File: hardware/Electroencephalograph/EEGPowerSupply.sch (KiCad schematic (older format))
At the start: 25 parts, among them U6 TPS60403, U7 LP5912-1.8DRVT, U8 LP5912-1.8DRVT, U9 LP5912-1.8DRVT

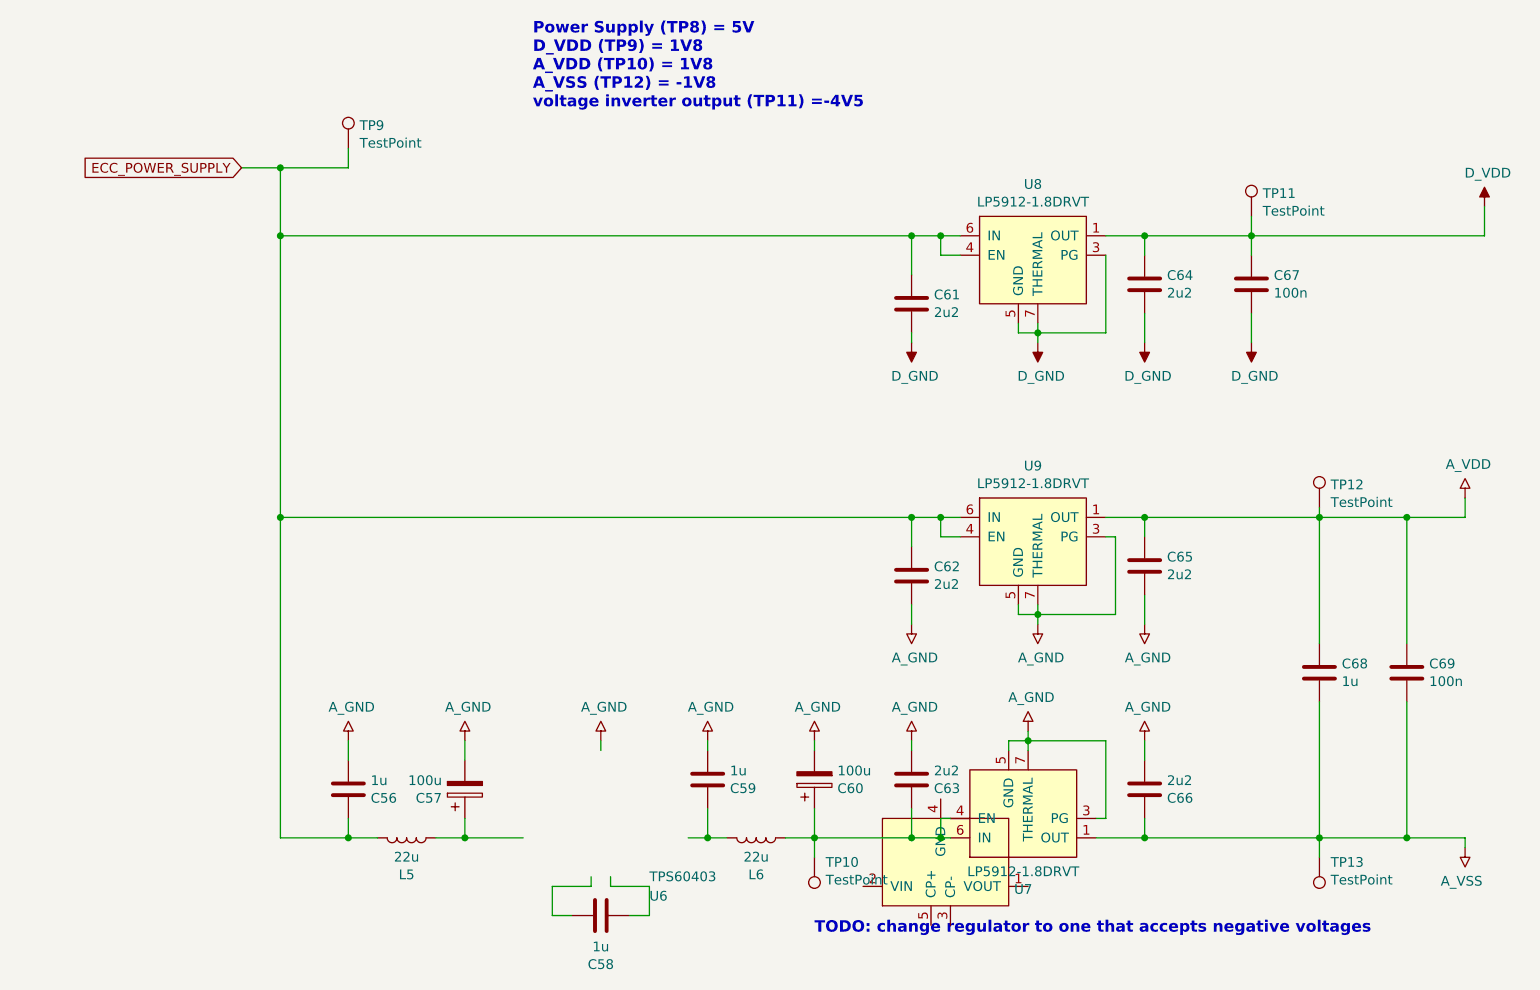
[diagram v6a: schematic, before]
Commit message: placing components groups
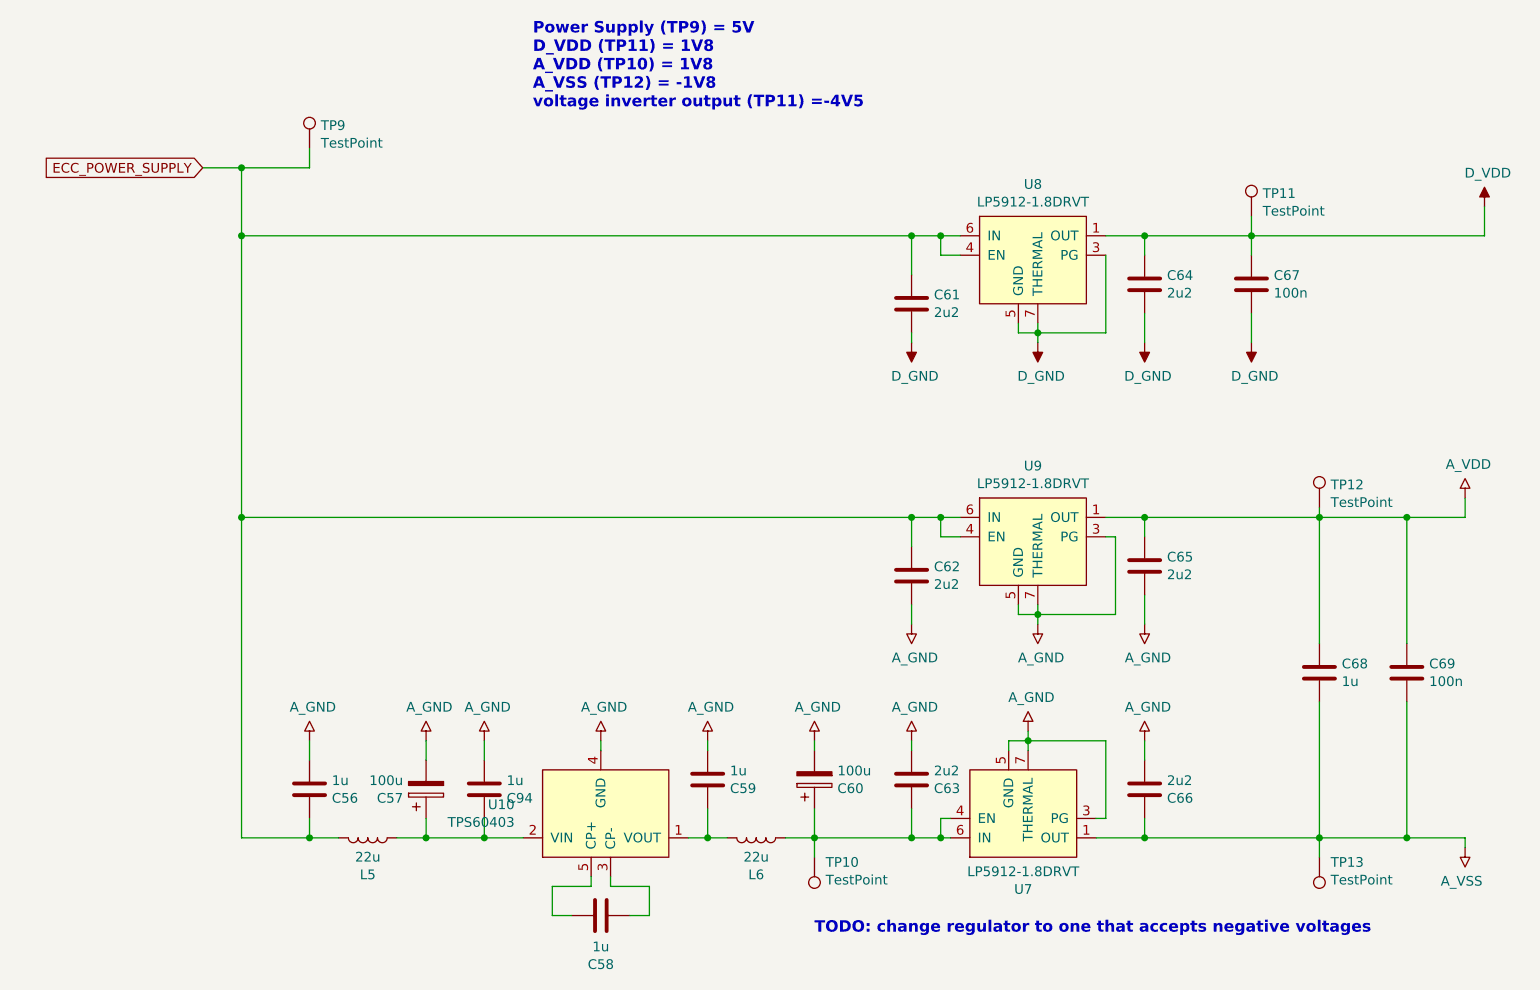
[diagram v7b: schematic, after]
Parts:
- removed U6: TPS60403, Package_SO:SOP-8_3.76x4.96mm_P1.27mm, symbol Electroencephalograph:TPS60403
- added C94: 1u, Capacitor_SMD:C_0402_1005Metric, symbol Device:C
- added U10: TPS60403, Package_TO_SOT_SMD:SOT-23-5, symbol Electroencephalograph:TPS60403
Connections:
- wire segments 101 -> 104
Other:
- note added: "Power Supply (TP9) = 5V\nD_VDD (TP11) = 1V8\nA_VDD (TP10) = 1V8\nA_VSS (TP12) = -1V8\nvoltage inverter output (TP11) =-4V5"
- note removed: "Power Supply (TP8) = 5V\nD_VDD (TP9) = 1V8\nA_VDD (TP10) = 1V8\nA_VSS (TP12) = -1V8\nvoltage inverter output (TP11) =-4V5"
- moved on the sheet: C56, C57, L5, TP9
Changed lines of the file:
@@
 $EndDescr
-$Comp
-L Electroencephalograph:TPS60403 U?
-U 1 1 5E0A0C58
-P 5450 5650
-AR Path="/5DFE0AD6/5E0A0C58" Ref="U?"  Part="1"
-AR Path="/5E0992D6/5E0A0C58" Ref="U6"  Part="1"
-F 0 "U6" H 3950 5800 50  0000 L CNN
-F 1 "TPS60403" H 3950 5700 50  0000 L CNN
-F 2 "Package_SO:SOP-8_3.76x4.96mm_P1.27mm" H 5450 5650 50  0001 C CNN
-F 3 "" H 5450 5650 50  0001 C CNN
-	1    5450 5650
-	1    0    0    1
-$EndComp
 $Comp
 L Device:C C?
@@
 	3750 5750 3750 5700
 Wire Wire Line
-	3300 5500 3000 5500
+	3300 5500 3100 5500
 Wire Wire Line
 	4150 5500 4250 5500
@@
 	4250 5000 4250 5050
 Wire Wire Line
-	3000 5500 3000 5400
-Wire Wire Line
-	3000 5000 3000 5100
+	2800 5500 2800 5400
+Wire Wire Line
+	2800 5000 2800 5100
 $Comp
 L Electroencephalograph:A_GND #PWR?
 U 1 1 5E0A0C8E
-P 3000 5000
+P 2800 5000
 AR Path="/5DFE0AD6/5E0A0C8E" Ref="#PWR?"  Part="1"
 AR Path="/5E0992D6/5E0A0C8E" Ref="#PWR111"  Part="1"
-F 0 "#PWR111" H 3000 5025 50  0001 C CNN
-F 1 "A_GND" H 3017 4827 50  0000 C CNN
-F 2 "" H 3000 5025 50  0001 C CNN
-F 3 "" H 3000 5025 50  0001 C CNN
-	1    3000 5000
+F 0 "#PWR111" H 2800 5025 50  0001 C CNN
+F 1 "A_GND" H 2817 4827 50  0000 C CNN
+F 2 "" H 2800 5025 50  0001 C CNN
+F 3 "" H 2800 5025 50  0001 C CNN
+	1    2800 5000
 	1    0    0    1
 $EndComp
@@
 L Device:C C?
 U 1 1 5E0A0C94
-P 2400 5250
+P 2200 5250
 AR Path="/5DF4CFF8/5E0A0C94" Ref="C?"  Part="1"
 AR Path="/5DF61103/5E0A0C94" Ref="C?"  Part="1"
 AR Path="/5DFE0AD6/5E0A0C94" Ref="C?"  Part="1"
 AR Path="/5E0992D6/5E0A0C94" Ref="C56"  Part="1"
-F 0 "C56" H 2515 5296 50  0000 L CNN
-F 1 "1u" H 2515 5205 50  0000 L CNN
-F 2 "Capacitor_SMD:C_0402_1005Metric" H 2438 5100 50  0001 C CNN
-F 3 "~" H 2400 5250 50  0001 C CNN
-	1    2400 5250
+F 0 "C56" H 2315 5296 50  0000 L CNN
+F 1 "1u" H 2315 5205 50  0000 L CNN
+F 2 "Capacitor_SMD:C_0402_1005Metric" H 2238 5100 50  0001 C CNN
+F 3 "~" H 2200 5250 50  0001 C CNN
+	1    2200 5250
 	1    0    0    1
 $EndComp
@@
 L Device:CP C?
 U 1 1 5E0A0C9A
-P 3000 5250
+P 2800 5250
 AR Path="/5DF4CFF8/5E0A0C9A" Ref="C?"  Part="1"
 AR Path="/5DF61103/5E0A0C9A" Ref="C?"  Part="1"
 AR Path="/5DFE0AD6/5E0A0C9A" Ref="C?"  Part="1"
 AR Path="/5E0992D6/5E0A0C9A" Ref="C57"  Part="1"
-F 0 "C57" H 2882 5296 50  0000 R CNN
-F 1 "100u" H 2882 5205 50  0000 R CNN
-F 2 "Capacitor_SMD:CP_Elec_6.3x5.8" H 3038 5100 50  0001 C CNN
-F 3 "~" H 3000 5250 50  0001 C CNN
-	1    3000 5250
+F 0 "C57" H 2682 5296 50  0000 R CNN
+F 1 "100u" H 2682 5205 50  0000 R CNN
+F 2 "Capacitor_SMD:CP_Elec_6.3x5.8" H 2838 5100 50  0001 C CNN
+F 3 "~" H 2800 5250 50  0001 C CNN
+	1    2800 5250
 	1    0    0    1
 $EndComp
@@
 L Electroencephalograph:A_GND #PWR?
 U 1 1 5E0A0CA6
-P 2400 5000
+P 2200 5000
 AR Path="/5DFE0AD6/5E0A0CA6" Ref="#PWR?"  Part="1"
 AR Path="/5E0992D6/5E0A0CA6" Ref="#PWR110"  Part="1"
-F 0 "#PWR110" H 2400 5025 50  0001 C CNN
-F 1 "A_GND" H 2417 4827 50  0000 C CNN
-F 2 "" H 2400 5025 50  0001 C CNN
-F 3 "" H 2400 5025 50  0001 C CNN
-	1    2400 5000
-	1    0    0    1
-$EndComp
-Wire Wire Line
-	2400 5000 2400 5100
-Wire Wire Line
-	2400 5400 2400 5500
+F 0 "#PWR110" H 2200 5025 50  0001 C CNN
+F 1 "A_GND" H 2217 4827 50  0000 C CNN
+F 2 "" H 2200 5025 50  0001 C CNN
+F 3 "" H 2200 5025 50  0001 C CNN
+	1    2200 5000
+	1    0    0    1
+$EndComp
+Wire Wire Line
+	2200 5000 2200 5100
+Wire Wire Line
+	2200 5400 2200 5500
 Wire Wire Line
 	4800 5500 4800 5350
@@
 Wire Wire Line
 	5300 5350 5300 5500
-Text GLabel 1850 2050 0    50   Input ~ 0
+Text GLabel 1650 2050 0    50   Input ~ 0
 ECC_POWER_SUPPLY
 $Comp
@@
 	5300 4000 5300 3850
 Wire Wire Line
-	1850 2050 2050 2050
-Wire Wire Line
-	2050 5500 2400 5500
-Wire Wire Line
-	2050 3850 5300 3850
-Connection ~ 2050 3850
-Wire Wire Line
-	2050 3850 2050 5500
+	1650 2050 1850 2050
+Wire Wire Line
+	1850 5500 2200 5500
+Wire Wire Line
+	1850 3850 5300 3850
+Connection ~ 1850 3850
+Wire Wire Line
+	1850 3850 1850 5500
 $Comp
 L Device:C C?
@@
 	8250 2400 8250 2250
 Wire Wire Line
-	5300 2400 2050 2400
-Wire Wire Line
-	2050 2050 2050 2400
+	5300 2400 1850 2400
+Wire Wire Line
+	1850 2050 1850 2400
 Connection ~ 5300 2400
-Connection ~ 2050 2400
-Wire Wire Line
-	2050 2400 2050 3850
+Connection ~ 1850 2400
+Wire Wire Line
+	1850 2400 1850 3850
 Connection ~ 5300 5500
 Wire Wire Line
@@
 L Device:L L?
 U 1 1 5E0C44DF
-P 2700 5500
+P 2500 5500
 AR Path="/5DFE0AD6/5E0C44DF" Ref="L?"  Part="1"
 AR Path="/5E0992D6/5E0C44DF" Ref="L5"  Part="1"
-F 0 "L5" V 2890 5500 50  0000 C CNN
-F 1 "22u" V 2799 5500 50  0000 C CNN
-F 2 "Electroencephalograph:L_7.3x7.3_H3.5" H 2700 5500 50  0001 C CNN
-F 3 "~" H 2700 5500 50  0001 C CNN
-	1    2700 5500
+F 0 "L5" V 2690 5500 50  0000 C CNN
+F 1 "22u" V 2599 5500 50  0000 C CNN
+F 2 "Electroencephalograph:L_7.3x7.3_H3.5" H 2500 5500 50  0001 C CNN
+F 3 "~" H 2500 5500 50  0001 C CNN
+	1    2500 5500
 	0    1    1    0
 $EndComp
 Wire Wire Line
-	2400 5500 2550 5500
-Connection ~ 2400 5500
-Wire Wire Line
-	2850 5500 3000 5500
-Connection ~ 3000 5500
+	2200 5500 2350 5500
+Connection ~ 2200 5500
+Wire Wire Line
+	2650 5500 2800 5500
+Connection ~ 2800 5500
 Wire Wire Line
 	6500 2400 7050 2400
@@
 Wire Wire Line
 	5950 4350 5950 4400
-Text Notes 3350 1750 0    59   ~ 12
-Power Supply (TP8) = 5V\nD_VDD (TP9) = 1V8\nA_VDD (TP10) = 1V8\nA_VSS (TP12) = -1V8\nvoltage inverter output (TP11) =-4V5
 $Comp
 L Electroencephalograph:A_GND #PWR?
@@
 	6250 5500 6500 5500
 Connection ~ 6500 5500
-$Comp
-L Connector:TestPoint TP?
-U 1 1 5E14A4FF
-P 2400 1950
-AR Path="/5DF61103/5E14A4FF" Ref="TP?"  Part="1"
-AR Path="/5E0992D6/5E14A4FF" Ref="TP9"  Part="1"
-F 0 "TP9" H 2458 2068 50  0000 L CNN
-F 1 "TestPoint" H 2458 1977 50  0000 L CNN
-F 2 "TestPoint:TestPoint_Pad_1.5x1.5mm" H 2600 1950 50  0001 C CNN
-F 3 "~" H 2600 1950 50  0001 C CNN
-	1    2400 1950
-	1    0    0    -1
-$EndComp
-Wire Wire Line
-	2050 2050 2400 2050
-Wire Wire Line
-	2400 2050 2400 1950
-Connection ~ 2050 2050
 Wire Wire Line
 	6500 5500 7400 5500
@@
 Text Notes 4800 6000 0    59   ~ 12
 TODO: change regulator to one that accepts negative voltages
+Wire Wire Line
+	2200 2050 2200 1950
+Connection ~ 1850 2050
+Wire Wire Line
+	1850 2050 2200 2050
+$Comp
+L Connector:TestPoint TP?
+U 1 1 5E14A4FF
+P 2200 1950
+AR Path="/5DF61103/5E14A4FF" Ref="TP?"  Part="1"
+AR Path="/5E0992D6/5E14A4FF" Ref="TP9"  Part="1"
+F 0 "TP9" H 2258 2068 50  0000 L CNN
+F 1 "TestPoint" H 2258 1977 50  0000 L CNN
+F 2 "TestPoint:TestPoint_Pad_1.5x1.5mm" H 2400 1950 50  0001 C CNN
+F 3 "~" H 2400 1950 50  0001 C CNN
+	1    2200 1950
+	1    0    0    -1
+$EndComp
+Text Notes 3350 1750 0    59   ~ 12
+Power Supply (TP9) = 5V\nD_VDD (TP11) = 1V8\nA_VDD (TP10) = 1V8\nA_VSS (TP12) = -1V8\nvoltage inverter output (TP11) =-4V5
+$Comp
+L Device:C C?
+U 1 1 5E0D7AE2
+P 3100 5250
+AR Path="/5DF4CFF8/5E0D7AE2" Ref="C?"  Part="1"
+AR Path="/5DF61103/5E0D7AE2" Ref="C?"  Part="1"
+AR Path="/5DFE0AD6/5E0D7AE2" Ref="C?"  Part="1"
+AR Path="/5E0992D6/5E0D7AE2" Ref="C94"  Part="1"
+F 0 "C94" H 3215 5296 50  0000 L CNN
+F 1 "1u" H 3215 5205 50  0000 L CNN
+F 2 "Capacitor_SMD:C_0402_1005Metric" H 3138 5100 50  0001 C CNN
+F 3 "~" H 3100 5250 50  0001 C CNN
+	1    3100 5250
+	1    0    0    1
+$EndComp
+$Comp
+L Electroencephalograph:A_GND #PWR?
+U 1 1 5E0D7AE8
+P 3100 5000
+AR Path="/5DFE0AD6/5E0D7AE8" Ref="#PWR?"  Part="1"
+AR Path="/5E0992D6/5E0D7AE8" Ref="#PWR176"  Part="1"
+F 0 "#PWR176" H 3100 5025 50  0001 C CNN
+F 1 "A_GND" H 3117 4827 50  0000 C CNN
+F 2 "" H 3100 5025 50  0001 C CNN
+F 3 "" H 3100 5025 50  0001 C CNN
+	1    3100 5000
+	1    0    0    1
+$EndComp
+Wire Wire Line
+	3100 5000 3100 5100
+Wire Wire Line
+	3100 5400 3100 5500
+Connection ~ 3100 5500
+Wire Wire Line
+	3100 5500 2800 5500
+$Comp
+L Electroencephalograph:TPS60403 U10
+U 1 1 5E0F81A7
+P 3700 5400
+F 0 "U10" H 3256 5329 50  0000 R CNN
+F 1 "TPS60403" H 3256 5420 50  0000 R CNN
+F 2 "Package_TO_SOT_SMD:SOT-23-5" H 4150 5700 50  0001 C CNN
+F 3 "http://www.ti.com/lit/ds/symlink/tps60402.pdf" H 4150 5700 50  0001 C CNN
+	1    3700 5400
+	1    0    0    1
+$EndComp
 $EndSCHEMATC
